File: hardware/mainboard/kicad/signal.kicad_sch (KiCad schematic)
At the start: 18 parts, among them J13 J_CAM, J14 J_LED, Q5 AO3400A, U8 74AHCT1G125, U9 74AHCT1G125

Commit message: Platine rev B geroutet: alle 134 Footprints platziert, DRC ohne Fehler, 3 offene Verbindungen; Renders und Lagenbilder; Fertigervergleich
- Lagen: In1 GND, B.Cu geteilte Versorgungsflaeche GND_PWR/5V_SYS, Plane-Vias an jedem SMD-Pad
- Freerouting 2.5.0 (JAR, Temurin 25) mit zwei Nachlaeufen auf fixierter Verdrahtung und kollisionsgeprueften Stummeln
- check_design.py: Netzliste gegen Spezifikation §4 (OK), make.sh fuer die ganze Kette
- 3D-Modelle Teensy 4.1 und XT30PW-M (CadQuery), Renders und layers.pdf in kicad/img
- Fertiger_2026-10-21.md: JLCPCB empfohlen, Aisler als EU-Rueckfall, BMP390 bei JLC nicht lieferbar
- naechster Schritt laut kicad/README.md §8: Review-Punkte A1-A5 (review_kicad_2026-10-21.md) vor dem Handrouting

Co-Authored-By: Claude Opus 5.5 <noreply@anthropic.com>
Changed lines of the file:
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@@
 		(company "Mission Space")
 		(comment 1 "WS2812B mit Pegelwandler, Summer, Kamera-Trigger")
-		(comment 2 "erzeugt von hardware/mainboard/kicad/gen_schematic.py aus circuit.py - nicht von Hand aendern")
+		(comment 2 "erzeugt aus circuit.py (gen_schematic.py)")
 	)
 	(text "WS2812B mit Pegelwandler, Summer, Kamera-Trigger"
@@
 		(stroke (width 0) (type default))
 	)
-	(label "LED1_5V"
+	(global_label "LED1_5V"
+		(shape passive)
 		(at 71.12 64.77 0)
 		(fields_autoplaced yes)
-		(effects (font (size 1.27 1.27)) (justify left bottom))
+		(effects (font (size 1.27 1.27)) (justify left))
 	)
 	(wire
@@
 		(stroke (width 0) (type default))
 	)
-	(label "LED1_5V"
+	(global_label "LED1_5V"
+		(shape passive)
 		(at 104.14 49.53 90)
 		(fields_autoplaced yes)
-		(effects (font (size 1.27 1.27)) (justify left bottom))
+		(effects (font (size 1.27 1.27)) (justify left))
 	)
 	(wire
@@
 		(stroke (width 0) (type default))
 	)
-	(label "LED1_DIN"
+	(global_label "LED1_DIN"
+		(shape passive)
 		(at 104.14 62.23 270)
 		(fields_autoplaced yes)
-		(effects (font (size 1.27 1.27)) (justify right bottom))
+		(effects (font (size 1.27 1.27)) (justify right))
 	)
 	(symbol
@@
 		(stroke (width 0) (type default))
 	)
-	(label "LED_EXT_DATA"
+	(global_label "LED_EXT_DATA"
+		(shape passive)
 		(at 147.32 62.23 0)
 		(fields_autoplaced yes)
-		(effects (font (size 1.27 1.27)) (justify left bottom))
+		(effects (font (size 1.27 1.27)) (justify left))
 	)
 	(wire
@@
 		(stroke (width 0) (type default))
 	)
-	(label "LED1_DIN"
+	(global_label "LED1_DIN"
+		(shape passive)
 		(at 127 62.23 180)
 		(fields_autoplaced yes)
-		(effects (font (size 1.27 1.27)) (justify right bottom))
+		(effects (font (size 1.27 1.27)) (justify right))
 	)
 	(wire
@@
 		(stroke (width 0) (type default))
 	)
-	(label "LED2_5V"
+	(global_label "LED2_5V"
+		(shape passive)
 		(at 87.63 113.03 0)
 		(fields_autoplaced yes)
-		(effects (font (size 1.27 1.27)) (justify left bottom))
+		(effects (font (size 1.27 1.27)) (justify left))
 	)
 	(wire
@@
 		(stroke (width 0) (type default))
 	)
-	(label "LED2_5V"
+	(global_label "LED2_5V"
+		(shape passive)
 		(at 120.65 97.79 90)
 		(fields_autoplaced yes)
-		(effects (font (size 1.27 1.27)) (justify left bottom))
+		(effects (font (size 1.27 1.27)) (justify left))
 	)
 	(wire
@@
 		(stroke (width 0) (type default))
 	)
-	(label "LED2_DIN"
+	(global_label "LED2_DIN"
+		(shape passive)
 		(at 120.65 110.49 270)
 		(fields_autoplaced yes)
-		(effects (font (size 1.27 1.27)) (justify right bottom))
+		(effects (font (size 1.27 1.27)) (justify right))
 	)
 	(symbol
@@
 		(stroke (width 0) (type default))
 	)
-	(label "LED2_DIN"
+	(global_label "LED2_DIN"
+		(shape passive)
 		(at 144.78 110.49 180)
 		(fields_autoplaced yes)
-		(effects (font (size 1.27 1.27)) (justify right bottom))
+		(effects (font (size 1.27 1.27)) (justify right))
 	)
 	(wire
@@
 		(stroke (width 0) (type default))
 	)
-	(label "LED_EXT_DATA"
+	(global_label "LED_EXT_DATA"
+		(shape passive)
 		(at 58.42 143.51 180)
 		(fields_autoplaced yes)
-		(effects (font (size 1.27 1.27)) (justify right bottom))
+		(effects (font (size 1.27 1.27)) (justify right))
 	)
 	(wire
@@
 		(stroke (width 0) (type default))
 	)
-	(label "BZ_NEG"
+	(global_label "BZ_NEG"
+		(shape passive)
 		(at 187.96 48.26 180)
 		(fields_autoplaced yes)
-		(effects (font (size 1.27 1.27)) (justify right bottom))
+		(effects (font (size 1.27 1.27)) (justify right))
 	)
 	(symbol
@@
 		(stroke (width 0) (type default))
 	)
-	(label "BZ_NEG"
+	(global_label "BZ_NEG"
+		(shape passive)
 		(at 218.44 44.45 0)
 		(fields_autoplaced yes)
-		(effects (font (size 1.27 1.27)) (justify left bottom))
+		(effects (font (size 1.27 1.27)) (justify left))
 	)
 	(symbol
@@
 		(stroke (width 0) (type default))
 	)
-	(label "BZ_G"
+	(global_label "BZ_G"
+		(shape passive)
 		(at 238.76 59.69 180)
 		(fields_autoplaced yes)
-		(effects (font (size 1.27 1.27)) (justify right bottom))
+		(effects (font (size 1.27 1.27)) (justify right))
 	)
 	(wire
@@
 		(stroke (width 0) (type default))
 	)
-	(label "BZ_NEG"
+	(global_label "BZ_NEG"
+		(shape passive)
 		(at 248.92 52.07 90)
 		(fields_autoplaced yes)
-		(effects (font (size 1.27 1.27)) (justify left bottom))
+		(effects (font (size 1.27 1.27)) (justify left))
 	)
 	(symbol
@@
 		(stroke (width 0) (type default))
 	)
-	(label "BZ_G"
+	(global_label "BZ_G"
+		(shape passive)
 		(at 256.54 60.96 270)
 		(fields_autoplaced yes)
-		(effects (font (size 1.27 1.27)) (justify right bottom))
+		(effects (font (size 1.27 1.27)) (justify right))
 	)
 	(symbol
@@
 		(stroke (width 0) (type default))
 	)
-	(label "BZ_G"
+	(global_label "BZ_G"
+		(shape passive)
 		(at 270.51 45.72 90)
 		(fields_autoplaced yes)
-		(effects (font (size 1.27 1.27)) (justify left bottom))
+		(effects (font (size 1.27 1.27)) (justify left))
 	)
 	(wire
@@
 		(stroke (width 0) (type default))
 	)
-	(label "CAM_TRIG_OUT"
+	(global_label "CAM_TRIG_OUT"
+		(shape passive)
 		(at 294.64 63.5 270)
 		(fields_autoplaced yes)
-		(effects (font (size 1.27 1.27)) (justify right bottom))
+		(effects (font (size 1.27 1.27)) (justify right))
 	)
 	(symbol
@@
 		(stroke (width 0) (type default))
 	)
-	(label "CAM_TRIG_OUT"
+	(global_label "CAM_TRIG_OUT"
+		(shape passive)
 		(at 323.85 46.99 180)
 		(fields_autoplaced yes)
-		(effects (font (size 1.27 1.27)) (justify right bottom))
-	)
-	(wire
+		(effects (font (size 1.27 1.27)) (justify right))
+	)
+	(wire

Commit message: Kartonaut: Name, Missionsabzeichen, Bestückungsdruck neu, Lötstopp blau
- Projekt heißt Kartonaut (Karton + Astronaut); Flüge werden hochgezählt, Erstflug = Kartonaut 1
- Abzeichen als Polygone in hardware/mainboard/kicad/logo.py, SVGs in docs/brand/
- spacecode/ -> firmware/, Bodenstation-Repo groundcode -> kartonaut-ground (Links, .gitignore)
- gen_pcb.py silk: Bestückungsdruck nur neu setzen, auf der gerouteten Platine; 1,0 mm Schrift,
  freie Plätze statt Überlappungen, Kurznamen an den Steckern, Testpunkte mit Netznamen,
  kleines Abzeichen vorn; hinten Abzeichen 20 mm und Steckerbelegung
- Stackup JLC04161H-7628 mit blauem Lötstopp im Board, Renders mit Stackup-Farben
- DRC-Druckwarnungen 167 -> 14 (Rest aus Footprint-Umrissen)

Co-Authored-By: Claude Opus 5.5 <noreply@anthropic.com>
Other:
- company: Mission Space -> Kartonaut
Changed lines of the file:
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@@
 		(date "2026-10-21")
 		(rev "B")
-		(company "Mission Space")
+		(company "Kartonaut")
 		(comment 1 "WS2812B mit Pegelwandler, Summer, Kamera-Trigger")
 		(comment 2 "erzeugt aus circuit.py (gen_schematic.py)")

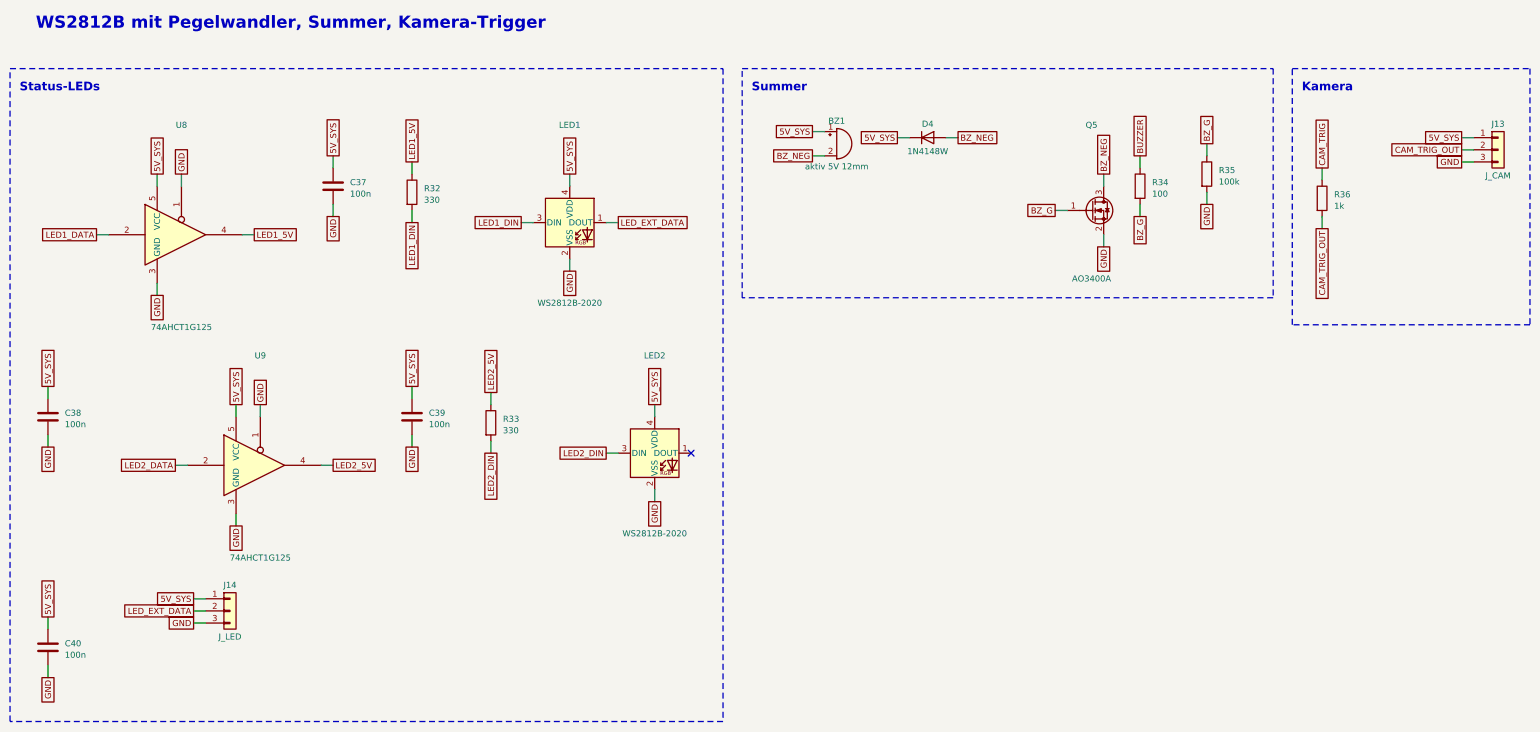
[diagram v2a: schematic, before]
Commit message: Mainboard rev B1: Review A1-A8 und Entscheidungen E1-E10 eingearbeitet, 2S-Pfad als F.Cu-Flaechen, 28 Verbindungen offen
Schaltung (circuit.py, ERC 0, Netzliste gegen README §4 OK): Hold-up hinter D1, EN-Teiler 330k/115k,
P-FET-Lastschalter je Akku, Polyfuse je Akku, Kelvin-Shunt mit INA239 an SPI1, BMP390 an SPI1,
74HC138/74HC4051 mit gemeinsamer Adresse, J_STACK 2x10 mit LDO 3V3_EXP, 1S-Lader MCP73831,
J_CHG2, vier Pyro-Kanaele (3/4 DNP), vierter Servo, alle Servos und Rollmotor an VSERVO,
3V3_SENS, eine WS2812B-Kette, Summer Pin 37, E22 NRST Pin 6; 166 Bauteile.

Platine (gen_pcb.py): neue Platzierung, 2S-Pfad, Pyro-Ausgaenge und VSYS_IN als F.Cu-Flaechen mit
Sperrflaechen fuer Freerouting, Strom-Klasse nur F.Cu, IMU-Zone 5 mm, patch mit Umweg ueber In2.
DRC 0 Fehler, Paritaet 0, kein 2S-Netz auf In2; 28 offene Verbindungen, Liste in kicad/README.md §5.5.
Spezifikation README.md und kicad/README.md auf B1 nachgezogen, review_check_layout.py fuer B1.

Co-Authored-By: Claude Opus 5.5 <noreply@anthropic.com>
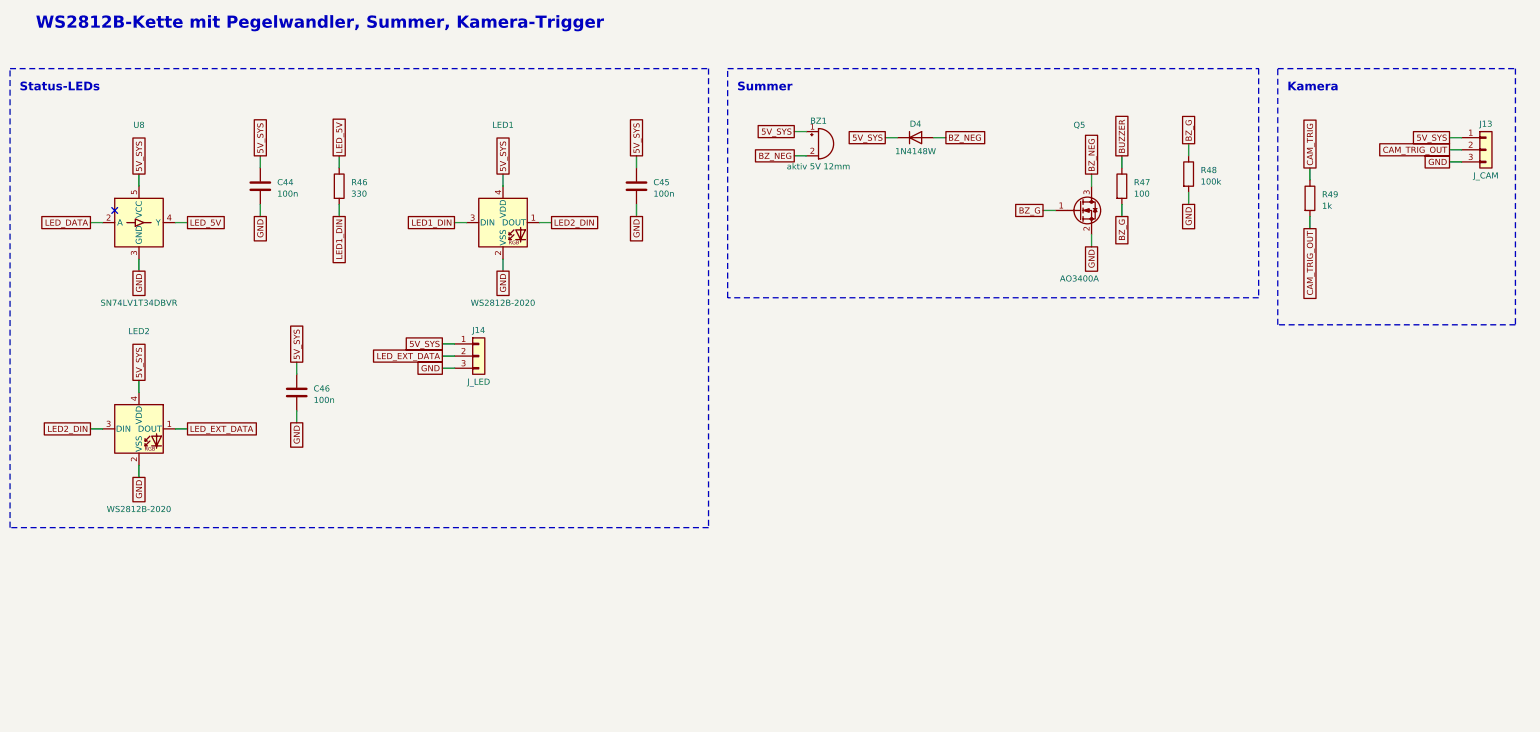
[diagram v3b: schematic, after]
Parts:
- removed C37, C38, C39, C40: 100n, Capacitor_SMD:C_0603_1608Metric, symbol Device:C
- removed R32, R33: 330, Resistor_SMD:R_0603_1608Metric, symbol Device:R
- removed R34: 100, Resistor_SMD:R_0603_1608Metric, symbol Device:R
- removed R35: 100k, Resistor_SMD:R_0603_1608Metric, symbol Device:R
- removed R36: 1k, Resistor_SMD:R_0603_1608Metric, symbol Device:R
- removed U9: 74AHCT1G125, Package_TO_SOT_SMD:SOT-23-5, symbol 74xGxx:74AHCT1G125
- added C44, C45, C46: 100n, Capacitor_SMD:C_0603_1608Metric, symbol Device:C
- added R46: 330, Resistor_SMD:R_0603_1608Metric, symbol Device:R
- added R47: 100, Resistor_SMD:R_0603_1608Metric, symbol Device:R
- added R48: 100k, Resistor_SMD:R_0603_1608Metric, symbol Device:R
- added R49: 1k, Resistor_SMD:R_0603_1608Metric, symbol Device:R
- U8: value 74AHCT1G125 -> SN74LV1T34DBVR; symbol 74xGxx:74AHCT1G125 -> Logic_LevelTranslator:SN74LV1T34DBV; LCSC C2870384 -> (none)
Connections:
- net 5V_SYS: now also C44.1, C45.1, C46.1
- net BUZZER: now also R47.1
- net BZ_G: now also R47.2, R48.1
- net CAM_TRIG: now also R49.1
- net CAM_TRIG_OUT: now also R49.2
- net GND: now also C44.2, C45.2, C46.2, R48.2; no longer U8.1
- net LED1_DIN: now also R46.2
- net LED2_DIN: now also LED1.1 (DOUT)
- net LED_EXT_DATA: now also LED2.1 (DOUT); no longer LED1.1 (DOUT)
- net LED1_5V renamed LED_5V
- net LED_5V: now also R46.1
- net LED1_DATA renamed LED_DATA
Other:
- note added: "WS2812B-Kette mit Pegelwandler, Summer, Kamera-Trigger"
- note removed: "WS2812B mit Pegelwandler, Summer, Kamera-Trigger"
- moved on the sheet: BZ1, D4, J13, J14, LED1, LED2, Q5
